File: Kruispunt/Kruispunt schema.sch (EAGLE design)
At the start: 87 parts, among them IC1 74ACT132N, IC2 LM555N, IC3 LM555N, IC4 74AC132N, IC5 786TV, Q1 BC548, Q10 BC548, Q2 2N3906, Q5 BC548, Q6 2N3906, Q9 BC548

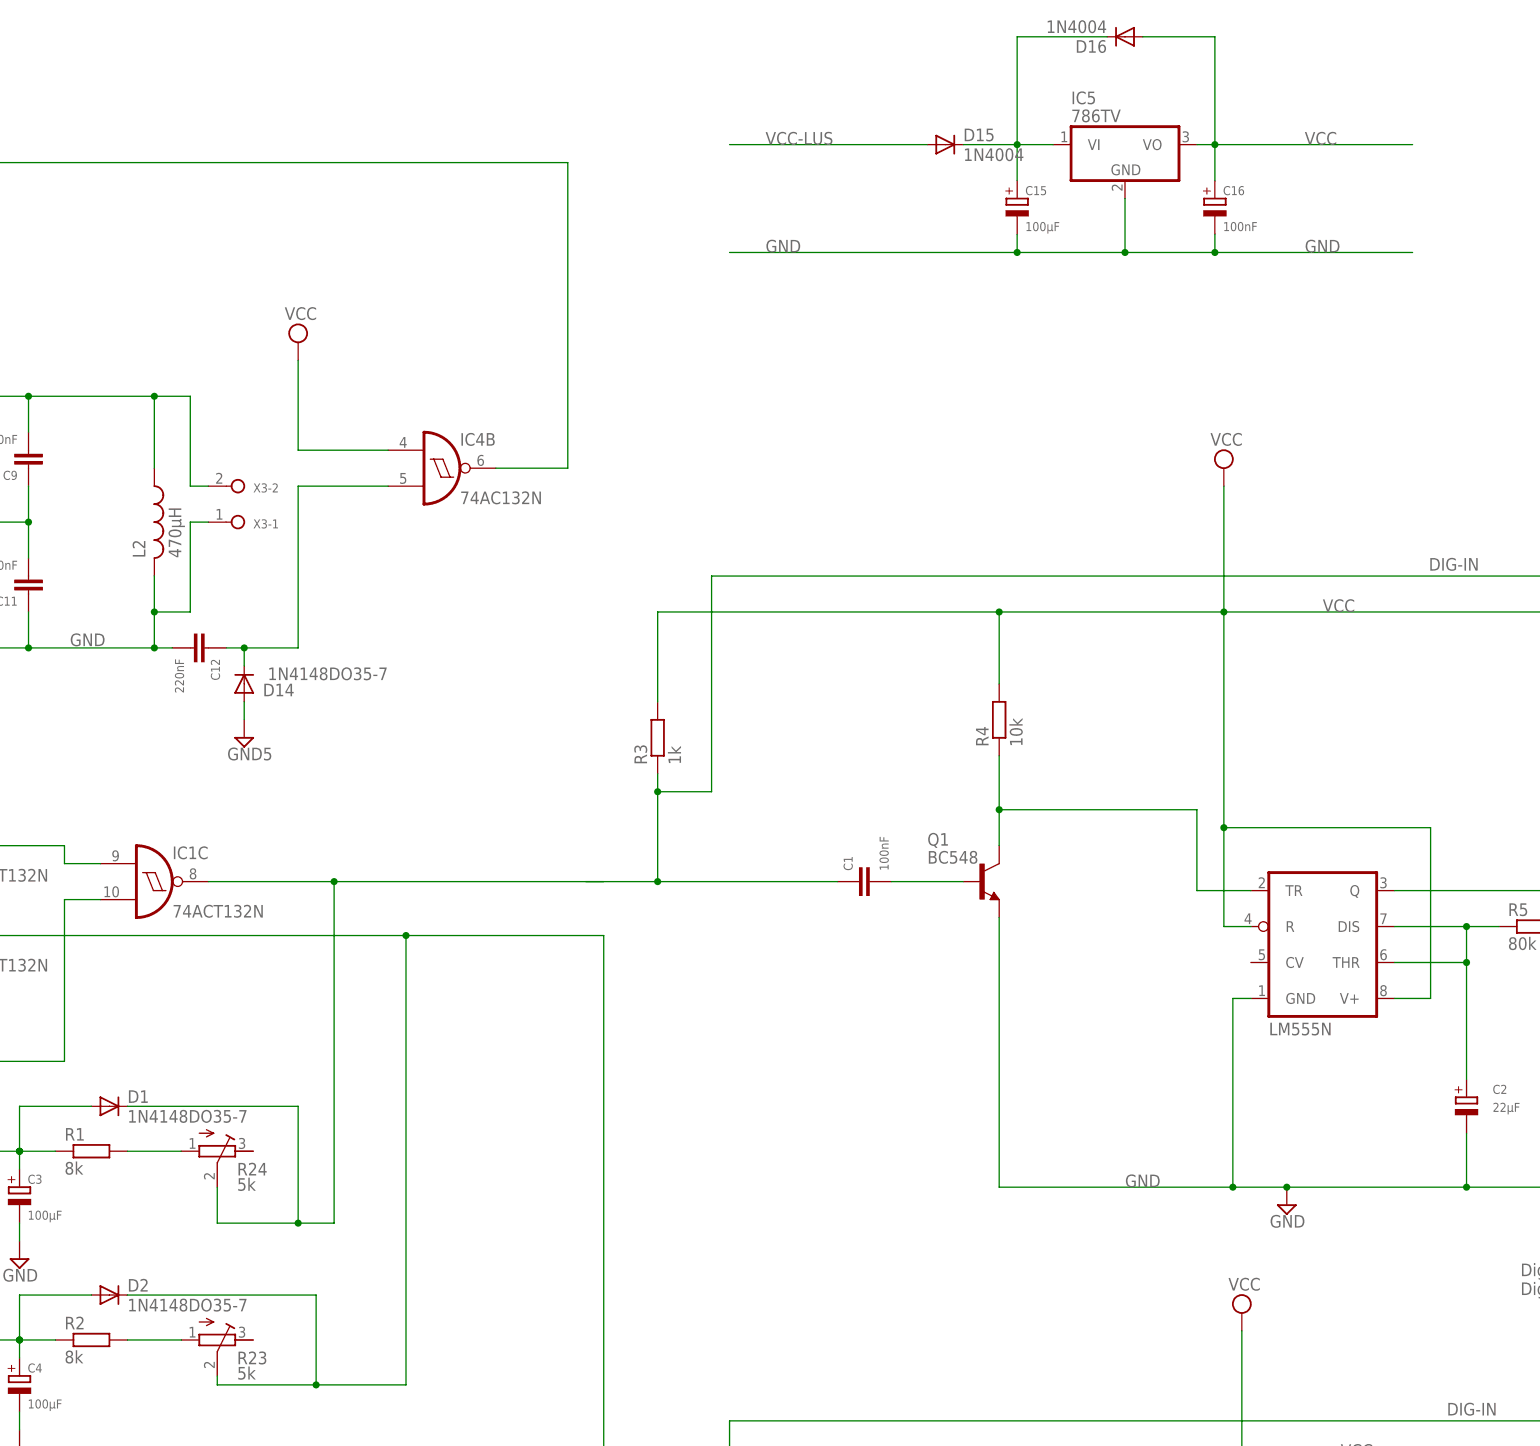
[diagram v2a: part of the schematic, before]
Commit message: Schema + logboek
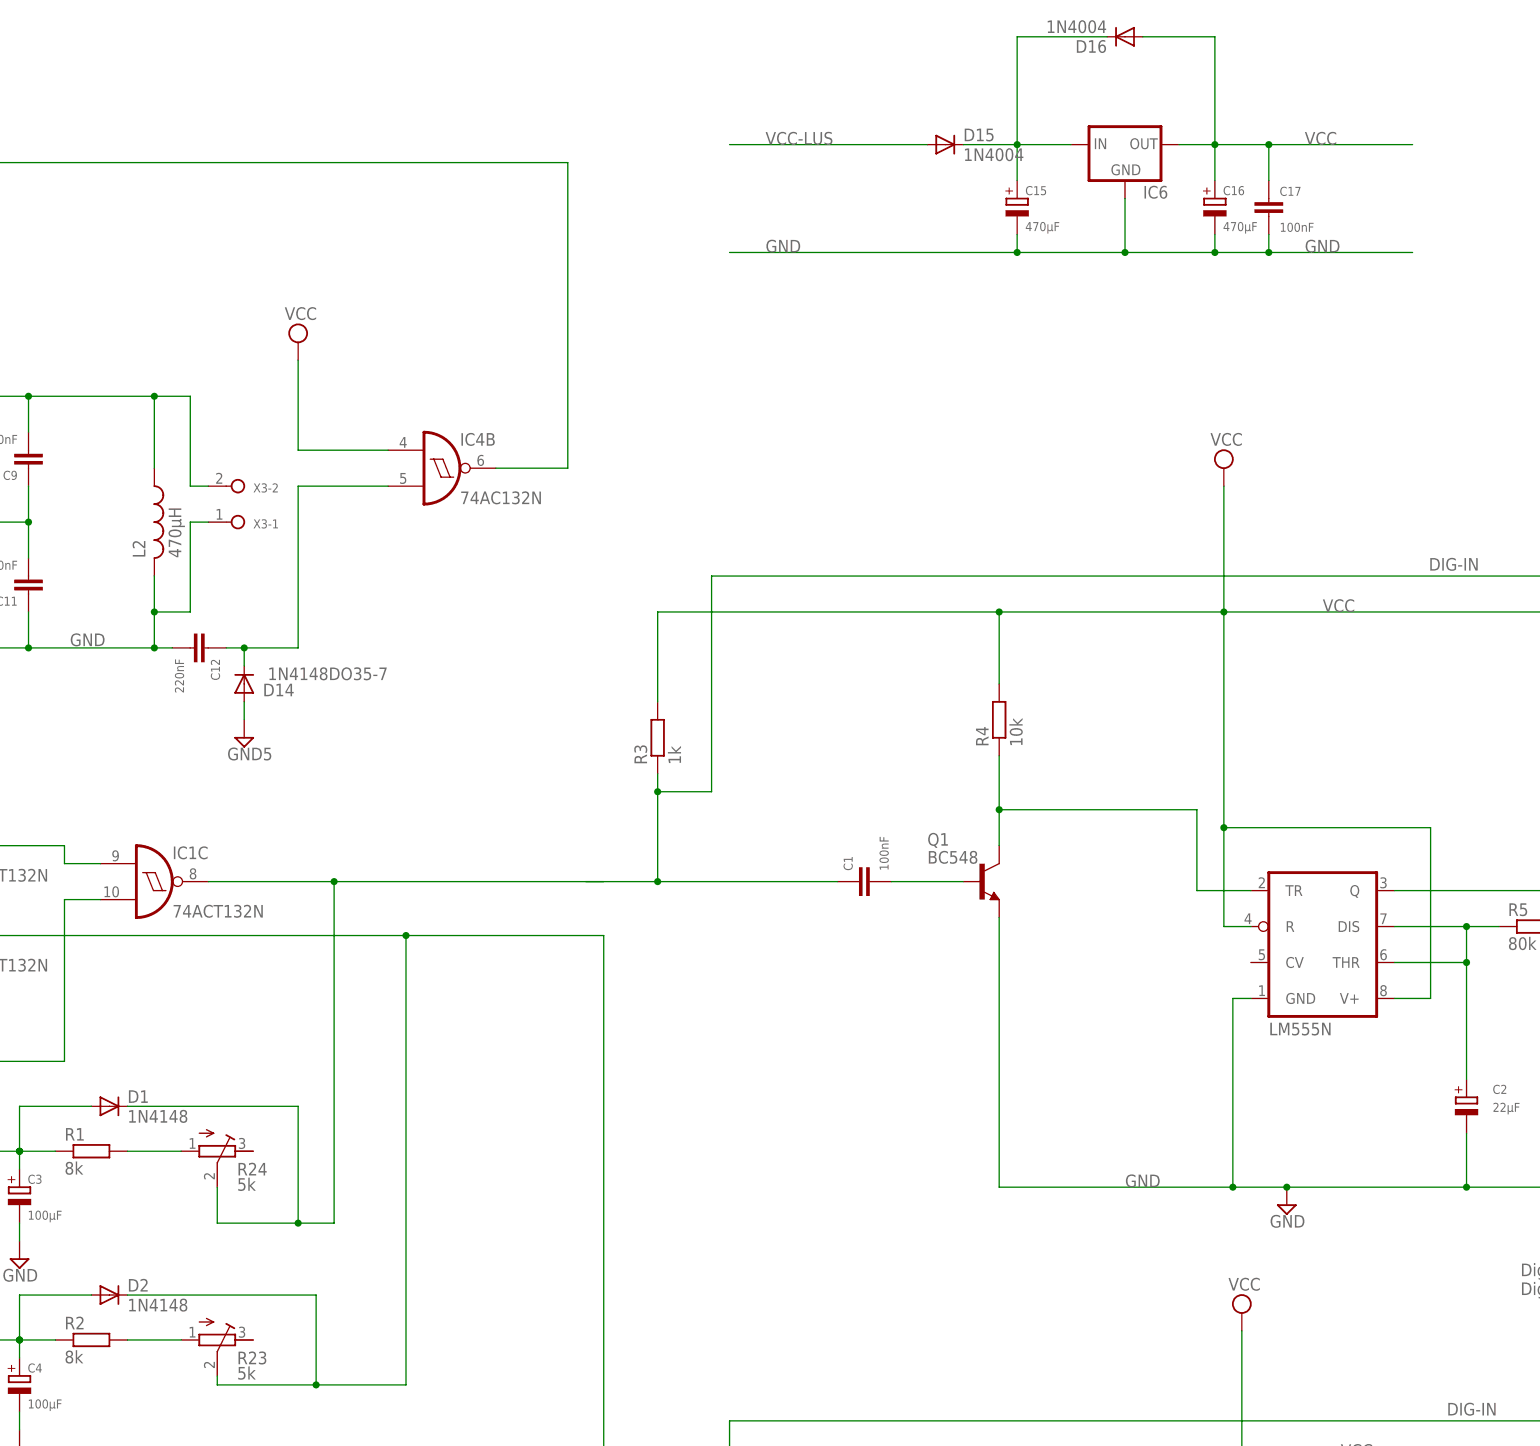
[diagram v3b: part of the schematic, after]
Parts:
- removed IC5: 786TV, Kruispunt Library:786TV
- added C17: 100nF, Kruispunt Library:CERAMIC-CAP3LEADS
- added IC6: (no value), Kruispunt Library:LM78XX-TO220LM78XX-HEATSINK
- C15: value 100µF -> 470µF; device Kruispunt Library:ELCOELCO2,5MMLEAD -> Kruispunt Library:ELCOELCO5,0MMLEAD
- C16: value 100nF -> 470µF; device Kruispunt Library:ELCOELCO2,5MMLEAD -> Kruispunt Library:ELCOELCO5,0MMLEAD
- D1, D2: value 1N4148DO35-7 -> 1N4148
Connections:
- net GND: now also C17.P$1, IC6.GND; no longer IC5.GND
- net N$45: now also IC6.IN; no longer IC5.VI
- net VCC: now also C17.P$2, IC6.OUT; no longer IC5.VO
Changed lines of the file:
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@@
 <class number="0" name="default" width="0" drill="0">
+</class>
+<class number="1" name="VCC" width="1.016" drill="0">
 </class>
 </classes>
@@
 <part name="R25" library="Kruispunt Library" deviceset="R-TRIMM" device="64W" value="50k"/>
 <part name="R26" library="Kruispunt Library" deviceset="R-TRIMM" device="64W" value="50k"/>
-<part name="D1" library="Kruispunt Library" deviceset="1N4148" device="DO35-7" package3d_urn="urn:adsk.eagle:package:43339/1"/>
-<part name="D2" library="Kruispunt Library" deviceset="1N4148" device="DO35-7" package3d_urn="urn:adsk.eagle:package:43339/1"/>
+<part name="D1" library="Kruispunt Library" deviceset="1N4148" device="DO35-7" package3d_urn="urn:adsk.eagle:package:43339/1" value="1N4148"/>
+<part name="D2" library="Kruispunt Library" deviceset="1N4148" device="DO35-7" package3d_urn="urn:adsk.eagle:package:43339/1" value="1N4148"/>
 <part name="D13" library="Kruispunt Library" deviceset="1N4148" device="DO35-7" package3d_urn="urn:adsk.eagle:package:43339/1"/>
 <part name="D5" library="Kruispunt Library" deviceset="1N4148" device="DO35-7" package3d_urn="urn:adsk.eagle:package:43339/1"/>
@@
 <part name="HOLE4" library="Kruispunt Library" deviceset="MOUNT-HOLE-4MM" device=""/>
 <part name="D15" library="Kruispunt Library" deviceset="1N4148" device="DO35-7" package3d_urn="urn:adsk.eagle:package:43339/1" value="1N4004"/>
-<part name="C15" library="Kruispunt Library" deviceset="ELCO" device="ELCO2,5MMLEAD" value="100µF"/>
-<part name="C16" library="Kruispunt Library" deviceset="ELCO" device="ELCO2,5MMLEAD" value="100nF"/>
+<part name="C15" library="Kruispunt Library" deviceset="ELCO" device="ELCO5,0MMLEAD" value="470µF"/>
+<part name="C16" library="Kruispunt Library" deviceset="ELCO" device="ELCO5,0MMLEAD" value="470µF"/>
 <part name="D16" library="Kruispunt Library" deviceset="1N4148" device="DO35-7" package3d_urn="urn:adsk.eagle:package:43339/1" value="1N4004"/>
-<part name="IC5" library="Kruispunt Library" deviceset="78*" device="TV" package3d_urn="urn:adsk.eagle:package:16417/1" technology="6"/>
+<part name="IC6" library="Kruispunt Library" deviceset="LM78XX-TO220" device="LM78XX-HEATSINK"/>
+<part name="C17" library="Kruispunt Library" deviceset="CERAMIC-CAP" device="3LEADS" value="100nF"/>
 </parts>
 <sheets>
@@
 <attribute name="VALUE" x="246.38" y="195.3514" size="1.778" layer="96" rot="R180"/>
 </instance>
-<instance part="IC5" gate="A1" x="248.92" y="177.8" smashed="yes">
-<attribute name="NAME" x="241.3" y="183.515" size="1.778" layer="95"/>
-<attribute name="VALUE" x="241.3" y="180.975" size="1.778" layer="96"/>
+<instance part="IC6" gate="1" x="248.92" y="177.8" smashed="yes">
+<attribute name="NAME" x="251.46" y="170.18" size="1.778" layer="95"/>
+<attribute name="VALUE" x="251.46" y="167.64" size="1.778" layer="96"/>
+</instance>
+<instance part="C17" gate="G$1" x="269.24" y="170.18" smashed="yes">
+<attribute name="NAME" x="270.764" y="170.561" size="1.27" layer="95"/>
+<attribute name="VALUE" x="270.764" y="165.481" size="1.27" layer="96"/>
 </instance>
 </instances>
@@
 </segment>
 </net>
-<net name="GND" class="0">
+<net name="GND" class="1">
 <segment>
 <pinref part="SUPPLY1" gate="G$1" pin="GND5"/>
@@
 <wire x1="261.62" y1="162.56" x2="248.92" y2="162.56" width="0.1524" layer="91"/>
 <junction x="248.92" y="162.56"/>
-<wire x1="261.62" y1="162.56" x2="289.56" y2="162.56" width="0.1524" layer="91"/>
+<wire x1="261.62" y1="162.56" x2="269.24" y2="162.56" width="0.1524" layer="91"/>
 <junction x="261.62" y="162.56"/>
 <label x="198.12" y="162.56" size="1.778" layer="95"/>
 <label x="274.32" y="162.56" size="1.778" layer="95"/>
-<pinref part="IC5" gate="A1" pin="GND"/>
+<pinref part="IC6" gate="1" pin="GND"/>
+<pinref part="C17" gate="G$1" pin="P$1"/>
+<wire x1="269.24" y1="162.56" x2="289.56" y2="162.56" width="0.1524" layer="91"/>
+<wire x1="269.24" y1="165.1" x2="269.24" y2="162.56" width="0.1524" layer="91"/>
+<junction x="269.24" y="162.56"/>
 </segment>
 </net>
@@
 </segment>
 </net>
-<net name="VCC" class="0">
+<net name="VCC" class="1">
 <segment>
 <wire x1="182.88" y1="99.06" x2="182.88" y2="111.76" width="0.1524" layer="91"/>
@@
 <pinref part="C16" gate="G$1" pin="+"/>
 <wire x1="261.62" y1="172.72" x2="261.62" y2="177.8" width="0.1524" layer="91"/>
-<wire x1="261.62" y1="177.8" x2="289.56" y2="177.8" width="0.1524" layer="91"/>
+<wire x1="261.62" y1="177.8" x2="269.24" y2="177.8" width="0.1524" layer="91"/>
 <label x="274.32" y="177.8" size="1.778" layer="95"/>
-<pinref part="IC5" gate="A1" pin="VO"/>
-<wire x1="259.08" y1="177.8" x2="261.62" y2="177.8" width="0.1524" layer="91"/>
 <junction x="261.62" y="177.8"/>
 <pinref part="D16" gate="G$1" pin="A"/>
+<wire x1="269.24" y1="177.8" x2="289.56" y2="177.8" width="0.1524" layer="91"/>
 <wire x1="261.62" y1="193.04" x2="251.46" y2="193.04" width="0.1524" layer="91"/>
 <wire x1="261.62" y1="193.04" x2="261.62" y2="177.8" width="0.1524" layer="91"/>
+<pinref part="IC6" gate="1" pin="OUT"/>
+<wire x1="256.54" y1="177.8" x2="261.62" y2="177.8" width="0.1524" layer="91"/>
+<pinref part="C17" gate="G$1" pin="P$2"/>
+<wire x1="269.24" y1="172.72" x2="269.24" y2="177.8" width="0.1524" layer="91"/>
+<junction x="269.24" y="177.8"/>
 </segment>
 </net>
@@
 </segment>
 </net>
-<net name="VCC-LUS" class="0">
+<net name="VCC-LUS" class="1">
 <segment>
 <wire x1="58.42" y1="-30.48" x2="58.42" y2="-27.94" width="0.1524" layer="91"/>
@@
 <pinref part="C15" gate="G$1" pin="+"/>
 <wire x1="233.68" y1="172.72" x2="233.68" y2="177.8" width="0.1524" layer="91"/>
-<pinref part="IC5" gate="A1" pin="VI"/>
-<wire x1="238.76" y1="177.8" x2="233.68" y2="177.8" width="0.1524" layer="91"/>
+<wire x1="241.3" y1="177.8" x2="233.68" y2="177.8" width="0.1524" layer="91"/>
 <junction x="233.68" y="177.8"/>
 <wire x1="233.68" y1="193.04" x2="233.68" y2="177.8" width="0.1524" layer="91"/>
-</segment>
-</net>
+<pinref part="IC6" gate="1" pin="IN"/>
+</segment>
+</net>

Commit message: logboek en schema
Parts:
- D10, D11, D13, D14, D5, D6: value 1N4148DO35-7 -> 1N4148
- IC2, IC3: device Hardware lichtsturing library:LM555N -> Kruispunt Library:LM555N
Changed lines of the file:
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@@
 <part name="C4" library="Kruispunt Library" deviceset="ELCO" device="ELCO2,5MMLEAD" value="100µF"/>
 <part name="IC1" library="Kruispunt Library" deviceset="74*132" device="N" package3d_urn="urn:adsk.eagle:package:2008/1" technology="ACT"/>
-<part name="IC2" library="Hardware lichtsturing library" deviceset="*555" device="N" technology="LM"/>
+<part name="IC2" library="Kruispunt Library" deviceset="*555" device="N" technology="LM"/>
 <part name="SUPPLY3" library="Hardware lichtsturing library" deviceset="VCC" device=""/>
 <part name="GND" library="Hardware lichtsturing library" deviceset="GND5" device="" value="GND"/>
@@
 <part name="D3" library="Hardware lichtsturing library" deviceset="TLLY4400" device="" package3d_urn="urn:adsk.eagle:package:15797/1" value="Rood"/>
 <part name="D7" library="Hardware lichtsturing library" deviceset="TLLY4400" device="" package3d_urn="urn:adsk.eagle:package:15797/1" value="Geel"/>
-<part name="IC3" library="Hardware lichtsturing library" deviceset="*555" device="N" technology="LM"/>
+<part name="IC3" library="Kruispunt Library" deviceset="*555" device="N" technology="LM"/>
 <part name="SUPPLY4" library="Hardware lichtsturing library" deviceset="VCC" device=""/>
 <part name="GND1" library="Hardware lichtsturing library" deviceset="GND5" device="" value="GND"/>
@@
 <part name="D1" library="Kruispunt Library" deviceset="1N4148" device="DO35-7" package3d_urn="urn:adsk.eagle:package:43339/1" value="1N4148"/>
 <part name="D2" library="Kruispunt Library" deviceset="1N4148" device="DO35-7" package3d_urn="urn:adsk.eagle:package:43339/1" value="1N4148"/>
-<part name="D13" library="Kruispunt Library" deviceset="1N4148" device="DO35-7" package3d_urn="urn:adsk.eagle:package:43339/1"/>
-<part name="D5" library="Kruispunt Library" deviceset="1N4148" device="DO35-7" package3d_urn="urn:adsk.eagle:package:43339/1"/>
-<part name="D6" library="Kruispunt Library" deviceset="1N4148" device="DO35-7" package3d_urn="urn:adsk.eagle:package:43339/1"/>
-<part name="D10" library="Kruispunt Library" deviceset="1N4148" device="DO35-7" package3d_urn="urn:adsk.eagle:package:43339/1"/>
-<part name="D11" library="Kruispunt Library" deviceset="1N4148" device="DO35-7" package3d_urn="urn:adsk.eagle:package:43339/1"/>
+<part name="D13" library="Kruispunt Library" deviceset="1N4148" device="DO35-7" package3d_urn="urn:adsk.eagle:package:43339/1" value="1N4148"/>
+<part name="D5" library="Kruispunt Library" deviceset="1N4148" device="DO35-7" package3d_urn="urn:adsk.eagle:package:43339/1" value="1N4148"/>
+<part name="D6" library="Kruispunt Library" deviceset="1N4148" device="DO35-7" package3d_urn="urn:adsk.eagle:package:43339/1" value="1N4148"/>
+<part name="D10" library="Kruispunt Library" deviceset="1N4148" device="DO35-7" package3d_urn="urn:adsk.eagle:package:43339/1" value="1N4148"/>
+<part name="D11" library="Kruispunt Library" deviceset="1N4148" device="DO35-7" package3d_urn="urn:adsk.eagle:package:43339/1" value="1N4148"/>
 <part name="SUPPLY7" library="Detectielus library" deviceset="VCC" device="" value="VCC-LUS"/>
 <part name="SUPPLY11" library="Detectielus library" deviceset="VCC" device="" value="VCC"/>
@@
 <part name="R30" library="Kruispunt Library" deviceset="RESISTOR" device="" value="2,2k"/>
 <part name="X3" library="Kruispunt Library" deviceset="TERMINAL-5MM-2POLE" device=""/>
-<part name="D14" library="Kruispunt Library" deviceset="1N4148" device="DO35-7" package3d_urn="urn:adsk.eagle:package:43339/1"/>
+<part name="D14" library="Kruispunt Library" deviceset="1N4148" device="DO35-7" package3d_urn="urn:adsk.eagle:package:43339/1" value="1N4148"/>
 <part name="IC4" library="Kruispunt Library" deviceset="74*132" device="N" package3d_urn="urn:adsk.eagle:package:2008/1" technology="AC"/>
 <part name="HOLE1" library="Kruispunt Library" deviceset="MOUNT-HOLE-4MM" device=""/>

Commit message: schema
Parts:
- added C18, C19: 10nF, Kruispunt Library:CERAMIC-CAP3LEADS
- added PAD1, PAD10, PAD11, PAD12, PAD13, PAD14, PAD15, PAD16, PAD17, PAD2, PAD3, PAD4, PAD5, PAD6, PAD7, PAD8, PAD9: Meetpin, Kruispunt Library:WIREPAD
- added X1: Geel1, Kruispunt Library:90-2
- added X10, X11: (no value), Kruispunt Library:90-2
- added X4: Rood1, Kruispunt Library:90-2
- added X6: Groen1, Kruispunt Library:90-2
- added X7: Geel2, Kruispunt Library:90-2
- added X8: Groen2, Kruispunt Library:90-2
- added X9: Rood2, Kruispunt Library:90-2
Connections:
- new net N$43: C18.P$2, IC2.CV
- new net N$46: ATTINY85.P4, X11.1
- new net N$49: D9.C, R16.1, X9.2
- net DIG-IN: now also D1.C, IC1C.O, PAD1.MOUNT, PAD2.MOUNT, R24.S, X1.2, X7.2
- net GND: now also C18.P$1, C19.P$1, PAD11.MOUNT, X10.2, X11.2, X6.1, X8.1
- net N$10: now also PAD17.MOUNT
- net N$11: now also X6.2
- net N$13: now also PAD12.MOUNT
- net N$14: now also X4.2
- net N$15: now also PAD8.MOUNT
- net N$17: now also PAD13.MOUNT
- net N$18: now also X1.1
- net N$20: now also PAD5.MOUNT
- net N$22: now also PAD16.MOUNT
- net N$23: now also X8.2
- net N$25: now also PAD14.MOUNT
- net N$26: now also ATTINY85.P3, X10.1; no longer D9.C, R16.1
- net N$27: now also PAD6.MOUNT
- net N$29: now also PAD15.MOUNT
- net N$30: now also X7.1
- net N$35: now also PAD4.MOUNT
- net N$38: now also C19.P$2, IC3.CV; no longer D1.C, IC1C.O, R24.S
- net N$44: now also PAD3.MOUNT
- net N$8: now also PAD7.MOUNT
- net VCC: now also PAD10.MOUNT, X4.1, X9.1
- net VCC-LUS: now also PAD9.MOUNT
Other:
- note added: "V2"
- moved on the sheet: C1, C11, C12, C15, C16, C17, C2, C3, C4, C8, C9, D1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

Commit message: schema
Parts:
- removed X7: Geel2, Kruispunt Library:90-2
- removed X8: Groen2, Kruispunt Library:90-2
- removed X9: Rood2, Kruispunt Library:90-2
- added X12, X13, X14: (no value), Kruispunt Library:TERMINAL-5MM-2POLE
- X1: value Geel1 -> (none); device Kruispunt Library:90-2 -> Kruispunt Library:TERMINAL-5MM-2POLE
- X10, X11: device Kruispunt Library:90-2 -> Kruispunt Library:TERMINAL-5MM-2POLE
- X4: value Rood1 -> (none); device Kruispunt Library:90-2 -> Kruispunt Library:TERMINAL-5MM-2POLE
- X6: value Groen1 -> (none); device Kruispunt Library:90-2 -> Kruispunt Library:TERMINAL-5MM-2POLE
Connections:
- net DIG-IN: now also X13-1.P$1, X6-1.P$1; no longer X1.2, X7.2
- net GND: now also X10-1.P$1, X11-1.P$1, X12-2.P$2, X14-2.P$2; no longer X10.2, X11.2, X6.1, X8.1
- net N$11: now also X12-1.P$1; no longer X6.2
- net N$14: now also X4-1.P$1; no longer X4.2
- net N$18: now also X13-2.P$2; no longer X1.1
- net N$23: now also X14-1.P$1; no longer X8.2
- net N$26: now also X10-2.P$2; no longer X10.1
- net N$30: now also X6-2.P$2; no longer X7.1
- net N$46: now also X11-2.P$2; no longer X11.1
- net N$49: now also X1-1.P$1; no longer X9.2
- net VCC: now also X1-2.P$2, X4-2.P$2; no longer X4.1, X9.1
